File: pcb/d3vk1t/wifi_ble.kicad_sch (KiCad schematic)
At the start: 1 part, among them U2 ESP32-C3-WROOM-02-H4

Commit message: [update all schematics sheets]
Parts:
- added C1 (x2): 100nF, Capacitor_SMD:C_0402_1005Metric, symbol Device:C_Small
- added C1: 22uF, Capacitor_SMD:C_0805_2012Metric, symbol Device:C_Small
- added J2: Conn_01x06, Connector_PinHeader_2.54mm:PinHeader_1x06_P2.54mm_Vertical, symbol Connector_Generic:Conn_01x06
- added Q1, Q2: MMBT2222, db:SOT23-BEC, symbol db-transistors:MMBT2222*
- added R1, R2, R3, R4, R5: 10K, Resistor_SMD:R_0402_1005Metric, symbol Device:R_Small
- added SW1: SW_Push, Button_Switch_SMD:SW_SPST_FSMSM, symbol Switch:SW_Push
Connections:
- net +3.3V: now reaches U2.1 (3V3)
- net +3.3V: now also C1.1, C1.1, J2.1 (Pin_1), R3.2, R5.2
- net ESP_RX: now reaches U2.11 (RXD)
- net ESP_RX: now also J2.6 (Pin_6)
- net ESP_TX: now reaches U2.12 (TXD)
- net ESP_TX: now also J2.5 (Pin_5)
- net GND: now reaches U2.19 (GND), U2.20 (GND), U2.21 (GND), U2.22 (GND), U2.23 (GND), U2.24 (GND), U2.25 (GND), U2.26 (GND), U2.27 (GND), U2.28 (GND), U2.29 (GND), U2.30 (GND), U2.31 (GND), U2.32 (GND), U2.33 (GND), U2.34 (GND), U2.35 (GND), U2.36 (GND), U2.37 (GND), U2.38 (GND), U2.39 (GND), U2.9 (GND)
- net GND: now also C1.2, C1.2, C1.2, J2.3 (Pin_3), R4.2
- net RESET: now reaches U2.2 (EN)
- net RESET: now also C1.1, Q1.C, R3.1
- net AT_TX: now reaches U2.5 (IO6)
- net AT_RX: now reaches U2.6 (IO7)
- net GPIO8: now reaches U2.7 (IO8)
- net GPIO8: now also R5.1
- net GPIO9: now reaches U2.8 (IO9)
- net GPIO9: now also Q2.C, SW1.1
- new net: R4.1, SW1.2
- new net: Q2.B, R2.2
- new net: Q1.B, R1.2
- new net DTR: J2.2 (Pin_2), Q2.E, R1.1
- new net RTS: J2.4 (Pin_4), Q1.E, R2.1
- no-connect marks 0 -> 9
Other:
- note added: "AUTO-RESET CIRCUIT"
- note added: "ESP32 - C3"
- note added: "ESP32 - FLASH"
- note added: "STRAPPING BITS - ESP32 - C3"
- moved on the sheet: U2

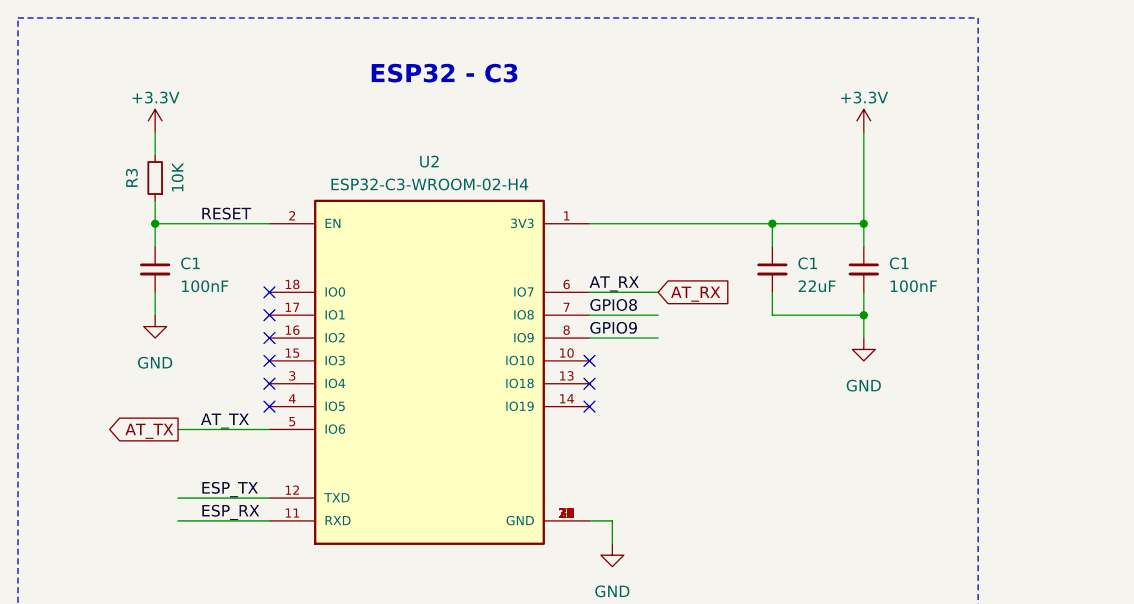
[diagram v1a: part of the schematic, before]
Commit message: sch: update all sch sheets.
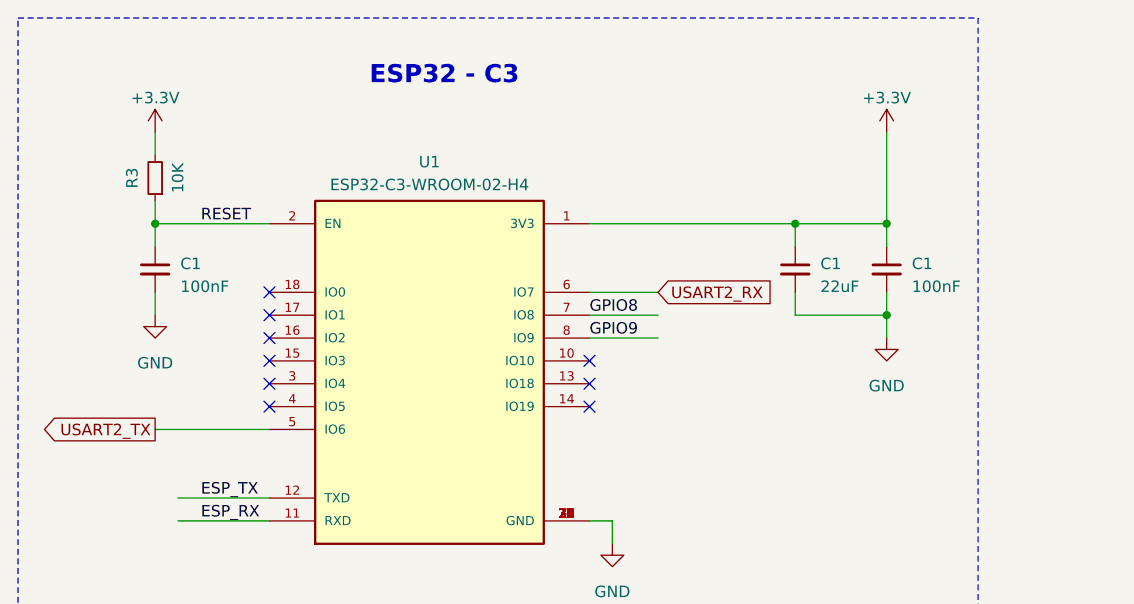
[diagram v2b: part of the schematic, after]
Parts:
- U1: renamed from U2; footprint MODULE_ESP32-C3-WROOM-02-H4 -> db:MODULE_ESP32-C3-WROOM-02-H4
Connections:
- net AT_RX renamed USART2_RX
- net AT_TX renamed USART2_TX
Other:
- moved on the sheet: C1

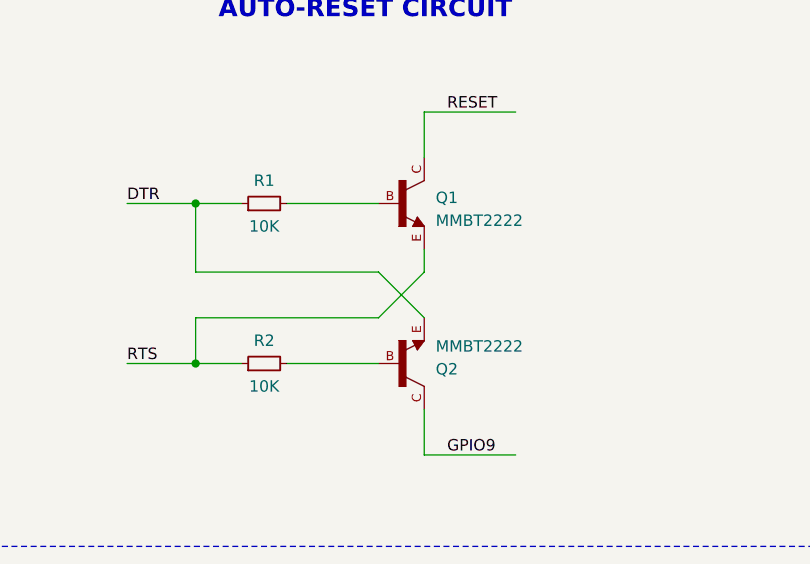
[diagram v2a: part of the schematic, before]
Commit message: pcb: update layout
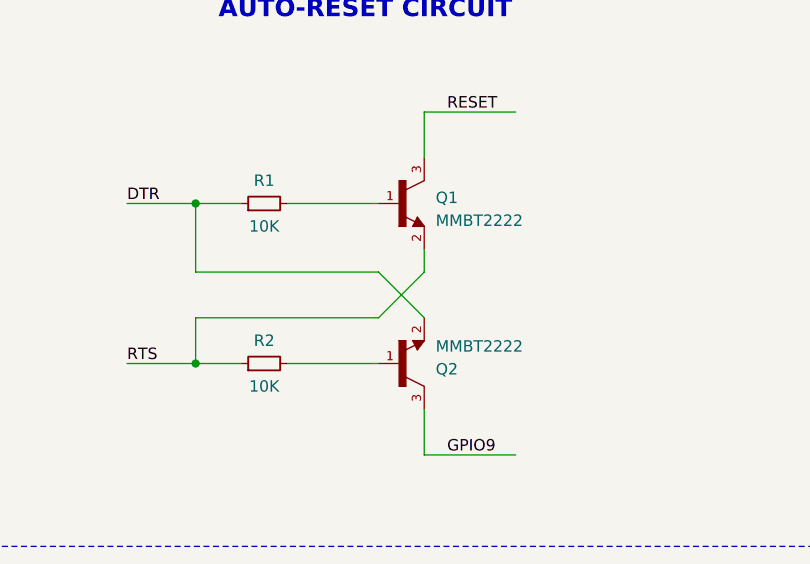
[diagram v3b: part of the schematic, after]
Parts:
- Q1, Q2: footprint db:SOT23-BEC -> bruno-libs:SOT-23B
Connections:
- net DTR: now also Q2.2; no longer Q2.E
- net GPIO9: now also Q2.3; no longer Q2.C
- net RESET: now also Q1.3; no longer Q1.C
- net RTS: now also Q1.2; no longer Q1.E
- net at R2.2: now also Q2.1; no longer Q2.B
- net at R1.2: now also Q1.1; no longer Q1.B
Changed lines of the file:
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@@
-    )
-  )
-  (symbol (lib_id "db-transistors:MMBT2222*") (at 81.28 139.7 0) (mirror x) (unit 1)
-    (in_bom yes) (on_board yes) (dnp no)
-    (property "Reference" "Q2" (at 85.09 140.335 0)
-      (effects (font (size 1.27 1.27)) (justify left))
-    )
-    (property "Value" "MMBT2222" (at 85.09 137.795 0)
-      (effects (font (size 1.27 1.27)) (justify left))
-    )
-    (property "Footprint" "db:SOT23-BEC" (at 81.28 139.7 0)
-      (effects (font (size 1.27 1.27)) (justify bottom) hide)
-    )
-    (property "Datasheet" "" (at 81.28 139.7 0)
-      (effects (font (size 1.27 1.27)) hide)
-    )
-    (pin "B")
-    (pin "C")
-    (pin "E")
-    (instances
-      (project "d3vk1t"
-        (path "/4ea523ae-7c45-478e-a9cc-6f4833d1a9d5/41f8e312-86c0-4917-8944-524577576fad"
-          (reference "Q2") (unit 1)
-        )
-      )
     )
   )
@@
     )
   )
-  (symbol (lib_id "db-transistors:MMBT2222*") (at 81.28 121.92 0) (unit 1)
+  (symbol (lib_name "MMBT2222*_1") (lib_id "db-transistors:MMBT2222*") (at 81.28 121.92 0) (unit 1)
     (in_bom yes) (on_board yes) (dnp no) (fields_autoplaced)
     (property "Reference" "Q1" (at 85.09 121.285 0)
@@
       (effects (font (size 1.27 1.27)) (justify left))
     )
-    (property "Footprint" "db:SOT23-BEC" (at 81.28 121.92 0)
+    (property "Footprint" "bruno-libs:SOT-23B" (at 81.28 121.92 0)
       (effects (font (size 1.27 1.27)) (justify bottom) hide)
     )
@@
       (effects (font (size 1.27 1.27)) hide)
     )
-    (pin "B")
-    (pin "C")
-    (pin "E")
+    (pin "1")
+    (pin "2")
+    (pin "3")
     (instances
       (project "d3vk1t"
@@
         )
       )
+    )
+  )
+  (symbol (lib_name "MMBT2222*_1") (lib_id "db-transistors:MMBT2222*") (at 81.28 139.7 0) (mirror x) (unit 1)
+    (in_bom yes) (on_board yes) (dnp no)
+    (property "Reference" "Q2" (at 85.09 140.335 0)
+      (effects (font (size 1.27 1.27)) (justify left))
+    )
+    (property "Value" "MMBT2222" (at 85.09 137.795 0)
+      (effects (font (size 1.27 1.27)) (justify left))
+    )
+    (property "Footprint" "bruno-libs:SOT-23B" (at 81.28 139.7 0)
+      (effects (font (size 1.27 1.27)) (justify bottom) hide)
+    )
+    (property "Datasheet" "" (at 81.28 139.7 0)
+      (effects (font (size 1.27 1.27)) hide)
+    )
+    (pin "1")
+    (pin "2")
+    (pin "3")
+    (instances
+      (project "d3vk1t"
+        (path "/4ea523ae-7c45-478e-a9cc-6f4833d1a9d5/41f8e312-86c0-4917-8944-524577576fad"
+          (reference "Q2") (unit 1)
+        )
+      )

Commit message: project update  - update pcb layout.  - update schmatics sheets.  - added manufacturing files.  - added documentation files.
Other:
- title: (none) -> Wi-Fi & Bluetooth Module
- moved on the sheet: J2
